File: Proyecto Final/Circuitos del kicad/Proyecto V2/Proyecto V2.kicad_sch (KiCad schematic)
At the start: 43 parts, among them J1 12v, Q1 PN2222A, Q2 PN2222A, Q3 PN2222A, SW1 SW_Push, SW2 SW_Push, SW3 SW_Push, SW4 SW_Push, U1 LM7805, U3 ATmega328P-P, Y1 16MHz

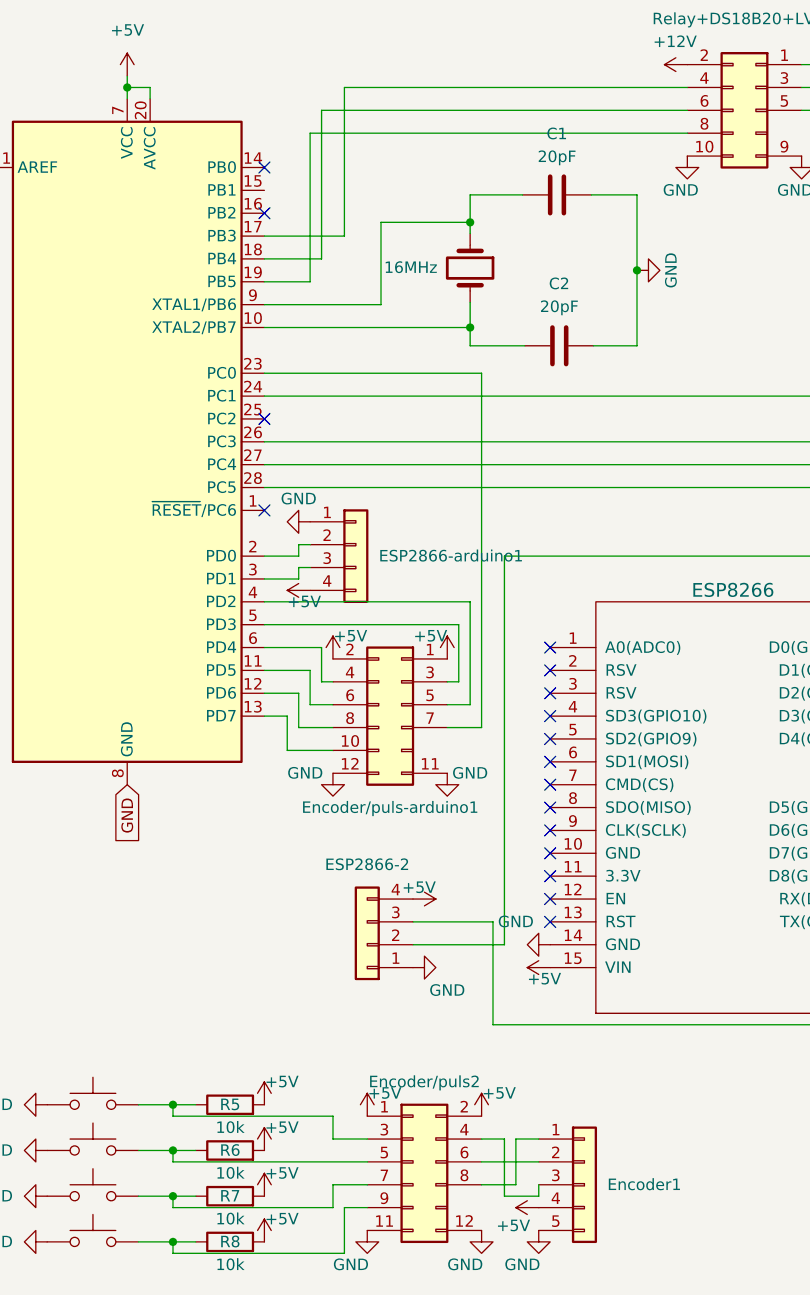
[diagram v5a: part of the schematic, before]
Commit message: IDC ESP + reset
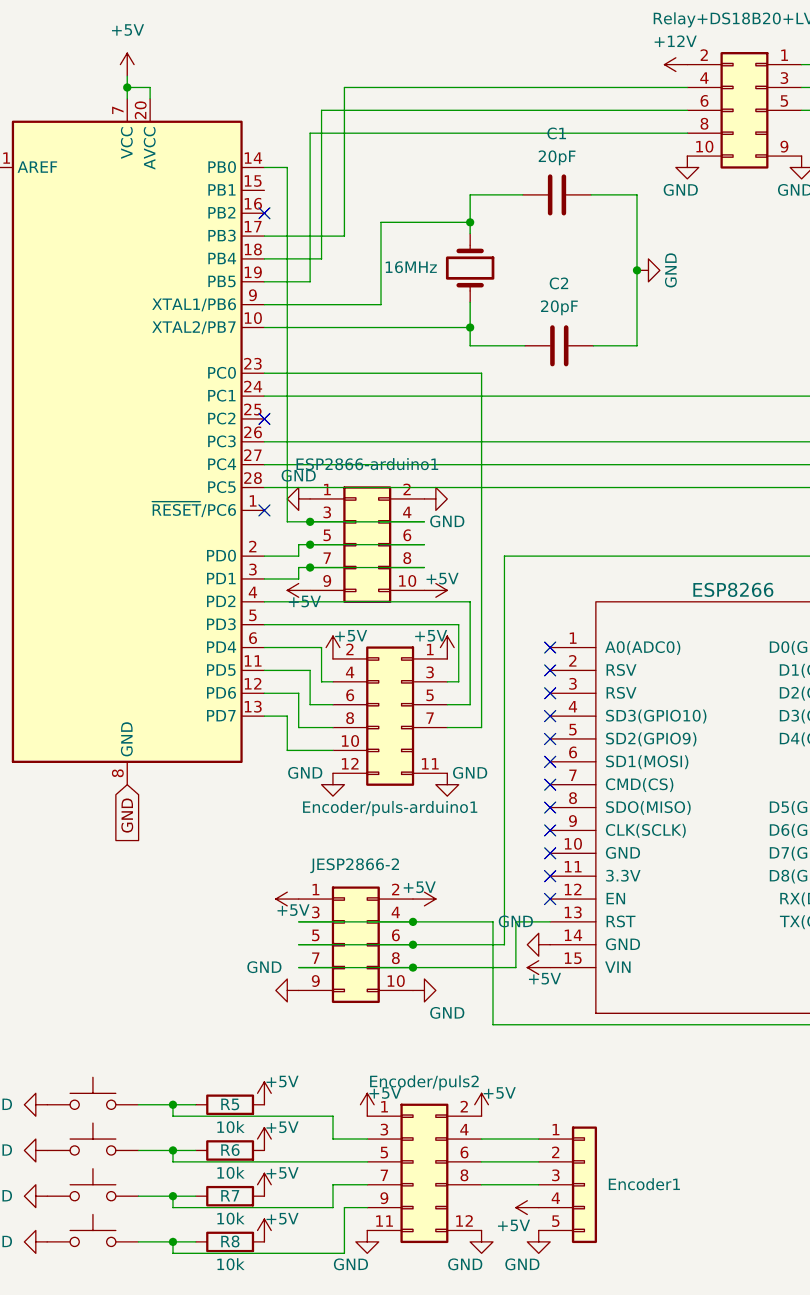
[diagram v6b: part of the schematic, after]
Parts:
- removed ESP2866-2, ESP2866-arduino1: Conn_01x04, Connector_PinHeader_2.54mm:PinHeader_1x04_P2.54mm_Vertical, symbol Connector_Generic:Conn_01x04
- added ESP2866-arduino1, JESP2866-2: Conn_02x05_Odd_Even, Connector_IDC:IDC-Header_2x05_P2.54mm_Vertical, symbol Connector_Generic:Conn_02x05_Odd_Even
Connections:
- net +5V: now also ESP2866-arduino1.10 (Pin_10), ESP2866-arduino1.9 (Pin_9), JESP2866-2.1 (Pin_1), JESP2866-2.2 (Pin_2)
- net GND: now also ESP2866-arduino1.1 (Pin_1), ESP2866-arduino1.2 (Pin_2), JESP2866-2.10 (Pin_10), JESP2866-2.9 (Pin_9)
- net at Encoder/puls2.4 (Pin_4): now also Encoder1.1 (Pin_1); no longer Encoder1.3 (Pin_3)
- net at Encoder/puls2.8 (Pin_8): now also Encoder1.3 (Pin_3); no longer Encoder1.1 (Pin_1)
- net at ESP8266.13 (RST): now also JESP2866-2.7 (Pin_7), JESP2866-2.8 (Pin_8)
- net at ESP8266.18 (TX(GPIO1)): now also JESP2866-2.3 (Pin_3), JESP2866-2.4 (Pin_4)
- net at ESP8266.19 (RX(DPIO3)): now also JESP2866-2.5 (Pin_5), JESP2866-2.6 (Pin_6)
- net at U3.2 (PD0): now also ESP2866-arduino1.5 (Pin_5), ESP2866-arduino1.6 (Pin_6)
- net at U3.3 (PD1): now also ESP2866-arduino1.7 (Pin_7), ESP2866-arduino1.8 (Pin_8)
- net at U3.14 (PB0): now also ESP2866-arduino1.3 (Pin_3), ESP2866-arduino1.4 (Pin_4)
- no-connect marks 34 -> 32
